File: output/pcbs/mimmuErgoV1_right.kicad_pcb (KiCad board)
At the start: 2 copper layers, 144.7 x 96.9 mm, 47 parts

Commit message: Add files via upload
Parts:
- moved D17 7.07 mm to (261.5, 216.1), turned to 27 degrees
- moved _4 7.04 mm to (250.6, 204.6), turned to 27 degrees
- moved S17 6.91 mm to (259.3, 211.7), turned to 27 degrees
- moved TRRS1 6.55 mm to (242.8, 179.7), turned to 102 degrees
- moved _3 6.39 mm to (261.5, 158.4), turned to 12 degrees
- moved _5 6.33 mm to (269.2, 211.4), turned to 27 degrees
- moved ROT1 6.19 mm to (253.5, 191.9), turned to 12 degrees
- moved MCU1 5.79 mm to (247.2, 160.3), turned to -78 degrees
- moved D16 5.65 mm to (278.3, 208.4), turned to 22 degrees
- moved S16 5.41 mm to (276.4, 203.7), turned to 22 degrees
- moved D3 4.83 mm to (366.7, 168.7), turned to -10 degrees
- moved S3 4.81 mm to (367.5, 163.8), turned to -10 degrees
- moved _10 4.61 mm to (338.9, 160.5), turned to -10 degrees
- moved _6 4.43 mm to (279.3, 191.6), turned to 22 degrees
- moved D13 4.41 mm to (274.8, 186.7), turned to 12 degrees
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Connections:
- D2 pad 1: P9 -> P6
- D3 pad 1: P6 -> P9
- ROT1 pad B: P3 -> P2
- ROT1 pad C: P2 -> P3
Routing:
- net P18: track 0.00 -> 179.0 mm
- net P6: track 0.00 -> 161.9 mm
- net P9: track 0.00 -> 156.1 mm
- net P8: track 0.00 -> 147.5 mm
- net P15: track 0.00 -> 140.2 mm
- net P16: track 0.00 -> 130.5 mm
- net P14: track 0.00 -> 113.9 mm
- net P7: track 0.00 -> 95.8 mm
- net P10: track 0.00 -> 89.1 mm
- net GND: track 0.00 -> 80.8 mm
- net P2: track 0.00 -> 42.2 mm
- net P19: track 0.00 -> 35.5 mm
- net P3: track 0.00 -> 35.0 mm
- net P20: track 0.00 -> 34.5 mm
- net VCC: track 0.00 -> 34.4 mm
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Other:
- board size 144.7 x 96.9 mm -> 146.2 x 102 mm
- net class Default removed

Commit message: finalize
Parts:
- moved D17 95.4 mm to (168.1, 197.0), turned to 21 degrees
- moved S17 95.0 mm to (166.3, 192.4), turned to 21 degrees
- moved _5 94.8 mm to (176.2, 193.1), turned to 21 degrees
- moved _4 94.4 mm to (158.4, 184.4), turned to 21 degrees
- moved D16 94.4 mm to (185.5, 191.0), turned to 16 degrees
- moved S16 93.9 mm to (184.1, 186.2), turned to 16 degrees
- moved ROT1 93.0 mm to (162.5, 172.1), turned to 6 degrees
- moved _6 92.6 mm to (188.3, 174.5), turned to 16 degrees
- moved D13 92.2 mm to (184.4, 169.1), turned to 6 degrees
- moved TRRS1 92.0 mm to (153.2, 158.8), turned to 96 degrees
- moved S13 91.7 mm to (183.8, 164.2), turned to 6 degrees
- moved D10 91.2 mm to (201.9, 164.3), turned to 6 degrees
- moved D1 91.0 mm to (255.6, 172.2), turned to -16 degrees
- moved D4 90.8 mm to (237.6, 167.1), turned to -6 degrees
- moved S10 90.8 mm to (201.4, 159.3), turned to 6 degrees
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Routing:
- net P10: track 89.1 -> 98.5 mm
- net GND: track 80.8 -> 71.9 mm, vias 0 -> 1
- net P6: track 161.9 -> 155.3 mm
- net P14: track 113.9 -> 119.0 mm
- net P15: track 140.2 -> 144.9 mm
- net P7: track 95.8 -> 91.2 mm
- net P8: track 147.5 -> 144.7 mm
- net P18: track 179.0 -> 181.8 mm
- net P16: track 130.5 -> 133.0 mm
- net mirror_ring_top: track 14.9 -> 16.9 mm
- net mirror_space_cluster: track 14.9 -> 16.8 mm
- net mirror_middle_top: track 14.9 -> 16.8 mm
- net mirror_pinkie_top: track 14.9 -> 16.8 mm
- net mirror_index_top: track 14.9 -> 16.8 mm
- net mirror_ring_bottom: track 14.9 -> 16.8 mm
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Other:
- board size 146.2 x 102 mm -> 144.3 x 95.7 mm
- board text added: "kubujuss v1"

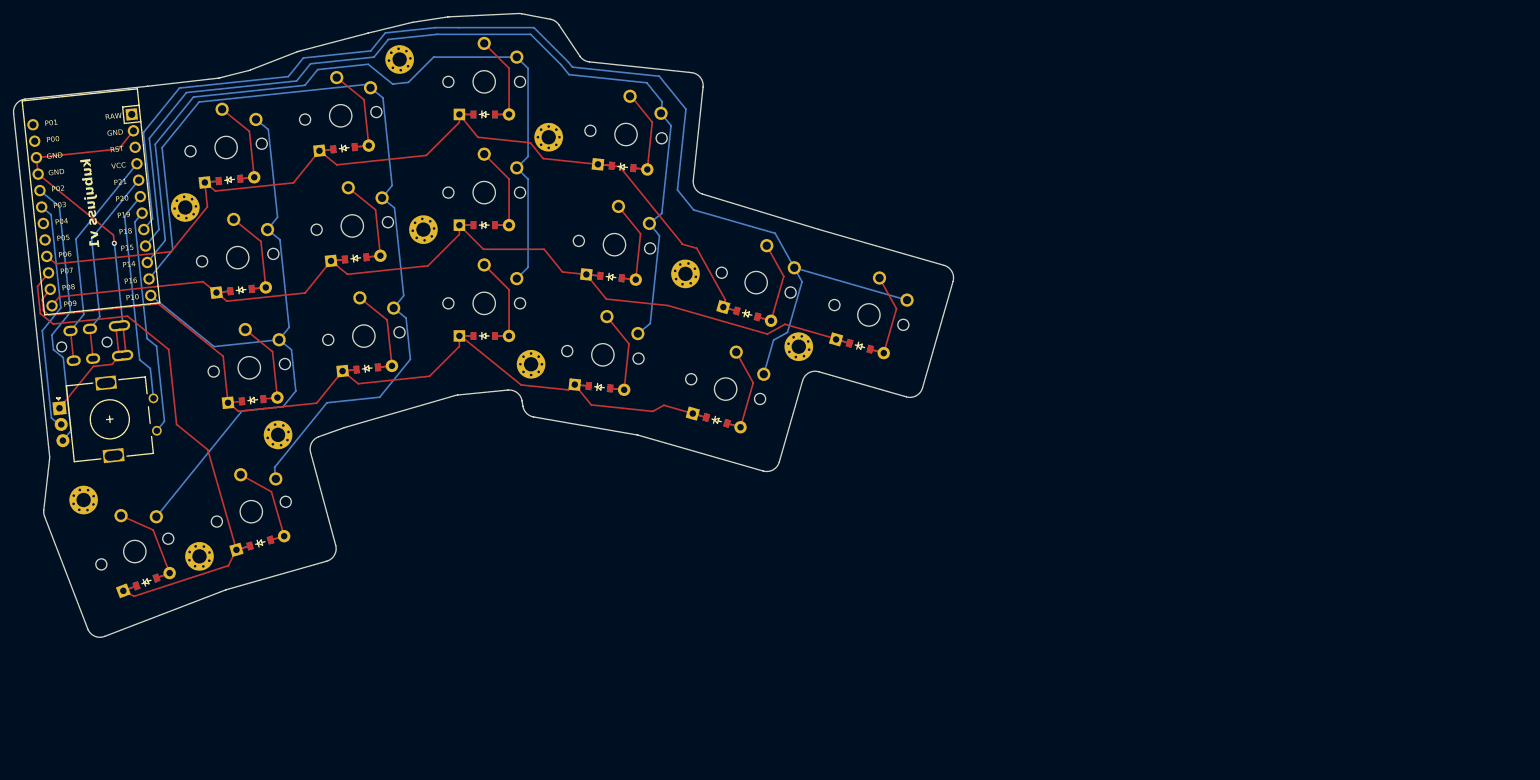
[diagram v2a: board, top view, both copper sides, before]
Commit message: Make GND and VCC traces 1mm thicker
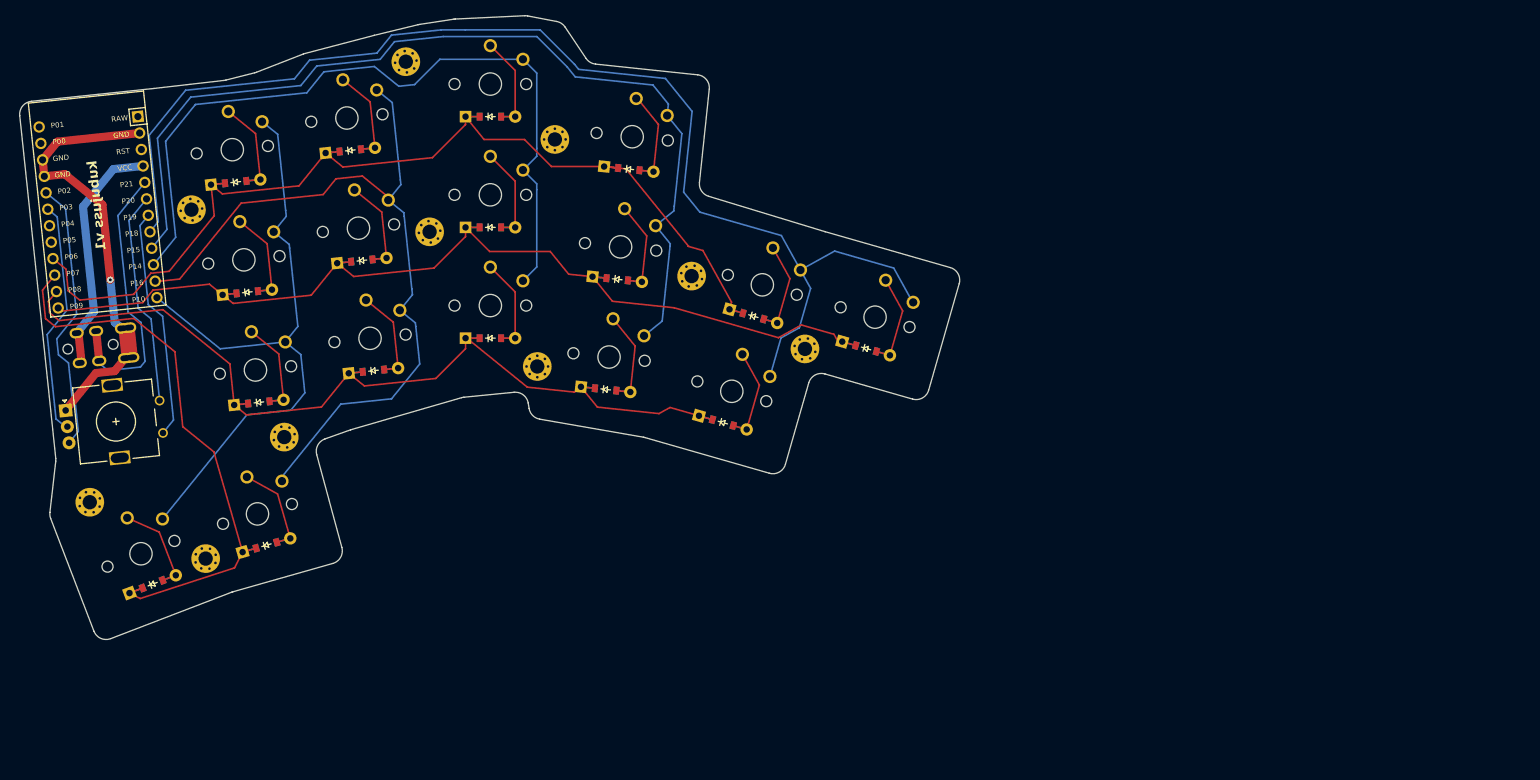
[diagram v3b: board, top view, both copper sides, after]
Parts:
- moved _8 1.00 mm to (228.0, 164.0)
- moved S15 1.00 mm to (181.2, 130.7)
- moved D3 1.00 mm to (278.5, 161.2)
- moved _5 1.00 mm to (177.1, 193.4)
- moved S1 1.00 mm to (257.9, 167.8)
- moved S3 1.00 mm to (279.9, 156.4)
- moved S7 1.00 mm to (220.8, 154.6)
- moved S9 1.00 mm to (220.8, 120.6)
- moved _7 1.00 mm to (211.5, 143.3)
- moved D2 1.00 mm to (261.2, 156.2)
- moved D6 1.00 mm to (242.1, 133.7)
- moved S14 1.00 mm to (183.0, 147.6)
- moved S13 1.00 mm to (184.8, 164.5)
- moved S10 1.00 mm to (202.4, 159.6)
- moved _10 1.00 mm to (251.7, 150.1)
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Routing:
- net P21: track 30.6 -> 42.8 mm
- net P16: track 133.0 -> 121.8 mm
- net P6: track 155.3 -> 162.9 mm
- net P18: track 181.8 -> 185.9 mm
- net VCC: track 34.4 -> 37.3 mm
- net GND: track 71.9 -> 74.1 mm
- net mirror_inner_bottom: track 14.6 -> 16.8 mm
- net P8: track 144.7 -> 146.4 mm
- net P10: track 98.5 -> 99.9 mm
- net P15: track 144.9 -> 146.2 mm
- net P9: track 156.8 -> 157.8 mm
- net P14: track 119.0 -> 119.6 mm
- net P19: track 35.1 -> 35.6 mm
- net P7: track 91.2 -> 91.7 mm
